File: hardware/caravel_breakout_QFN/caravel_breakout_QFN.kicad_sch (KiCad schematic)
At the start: 20 parts, among them J1 Conn_01x14_Female, J2 Conn_01x14_Female, J3 Conn_01x14_Female, J4 Conn_01x14_Female, T1 Logo, T2 Logo, U1 Caravel

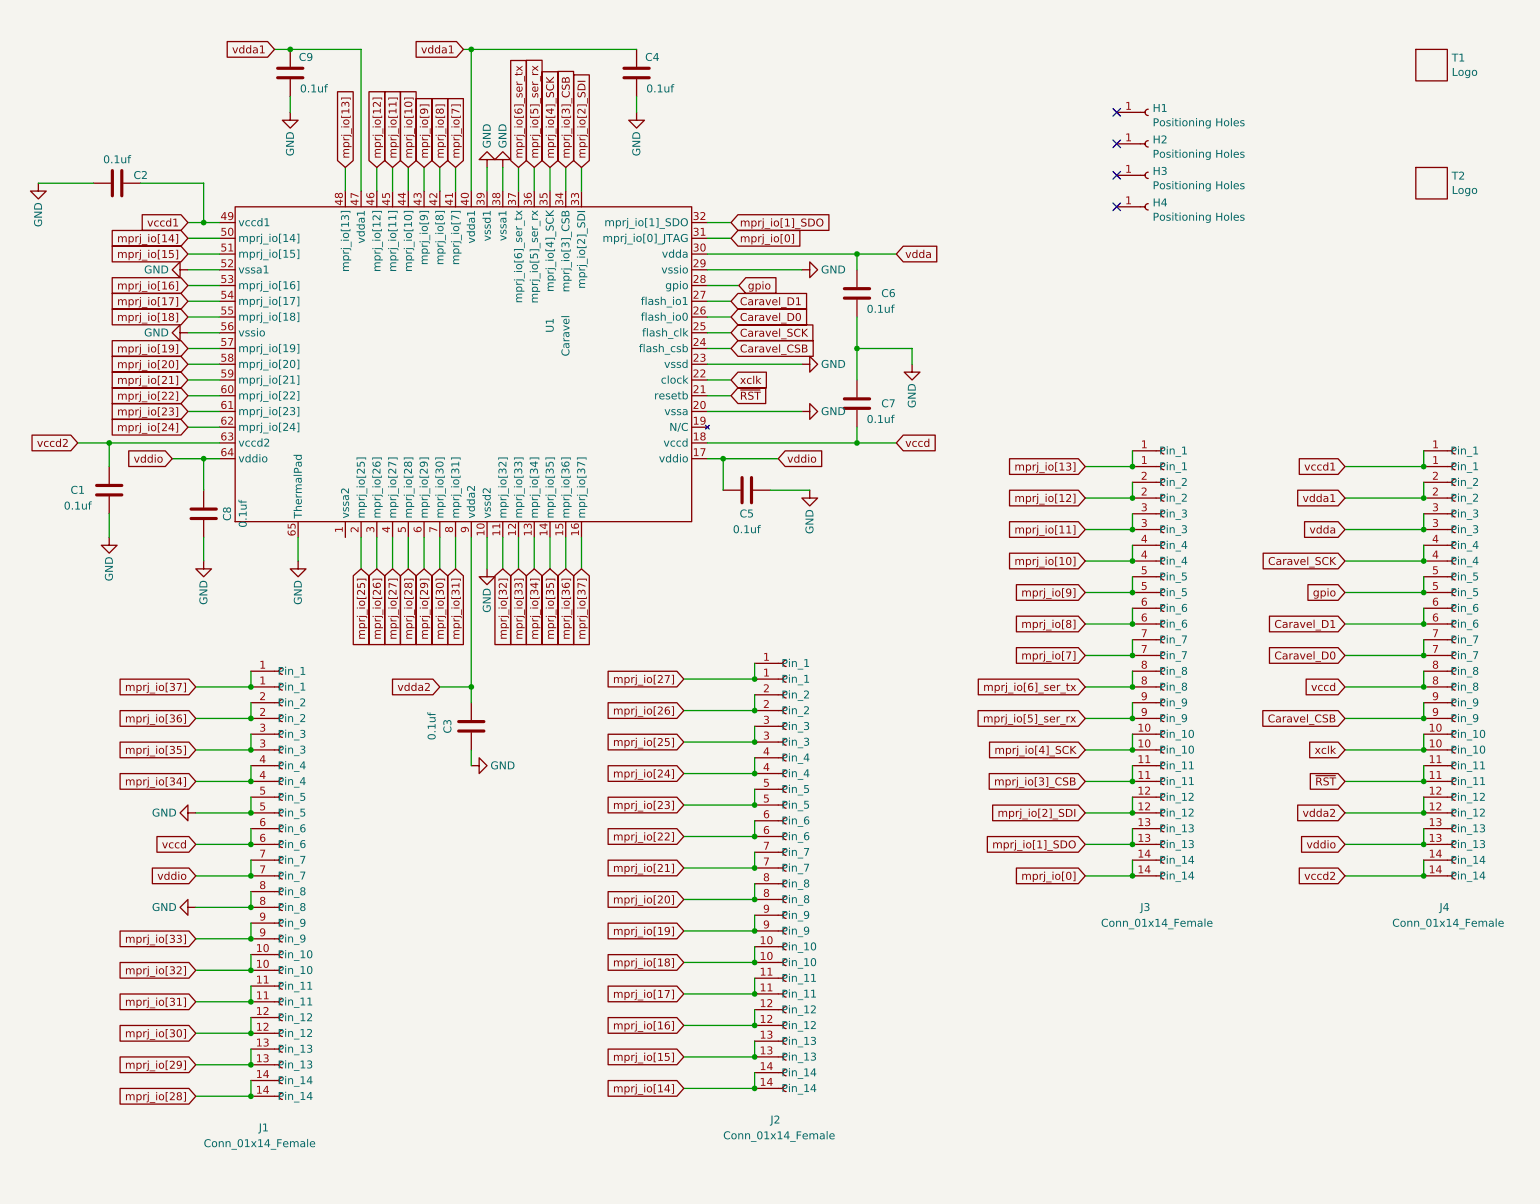
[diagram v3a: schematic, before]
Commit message: update caravel QFN breakout board with WCSP pinout (V2)
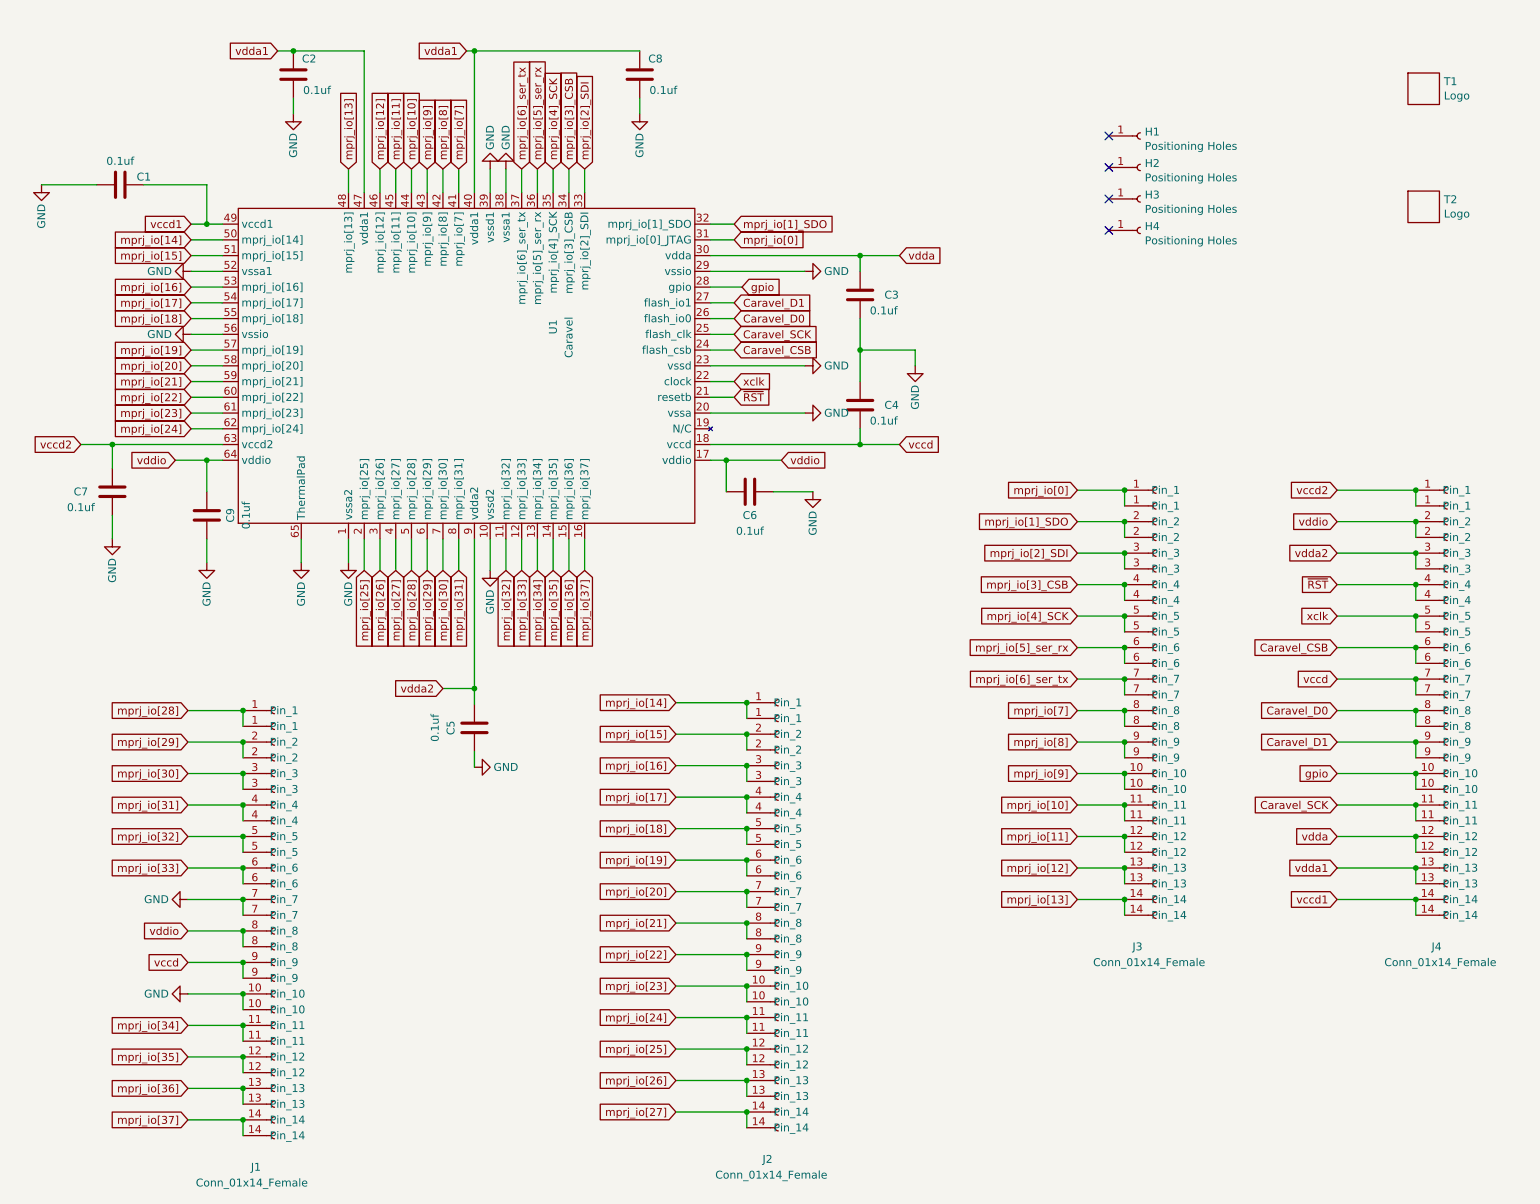
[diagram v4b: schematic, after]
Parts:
- U1: footprint Package_DFN_QFN:QFN-64-1EP_9x9mm_P0.5mm_EP7.65x7.65mm_ThermalVias -> Package_DFN_QFN:QFN-64-1EP_9x9mm_P0.5mm_EP7.65x7.65mm
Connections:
- net Caravel_CSB: now also J4.6 (Pin_6); no longer J4.9 (Pin_9)
- net Caravel_D0: now also J4.8 (Pin_8); no longer J4.7 (Pin_7)
- net Caravel_D1: now also J4.9 (Pin_9); no longer J4.6 (Pin_6)
- net Caravel_SCK: now also J4.11 (Pin_11); no longer J4.4 (Pin_4)
- net GND: now also C2.2, C3.2, C4.1, C6.1, C8.2, C9.1, J1.10 (Pin_10), J1.7 (Pin_7), U1.1 (vssa2); no longer C2.1, C3.1, C4.2, C6.2, C8.1, C9.2, J1.5 (Pin_5), J1.8 (Pin_8)
- net gpio: now also J4.10 (Pin_10); no longer J4.5 (Pin_5)
- net mprj_io[0]: now also J3.1 (Pin_1); no longer J3.14 (Pin_14)
- net mprj_io[10]: now also J3.11 (Pin_11); no longer J3.4 (Pin_4)
- net mprj_io[11]: now also J3.12 (Pin_12); no longer J3.3 (Pin_3)
- net mprj_io[12]: now also J3.13 (Pin_13); no longer J3.2 (Pin_2)
- net mprj_io[13]: now also J3.14 (Pin_14); no longer J3.1 (Pin_1)
- net mprj_io[14]: now also J2.1 (Pin_1); no longer J2.14 (Pin_14)
- net mprj_io[15]: now also J2.2 (Pin_2); no longer J2.13 (Pin_13)
- net mprj_io[16]: now also J2.3 (Pin_3); no longer J2.12 (Pin_12)
- net mprj_io[17]: now also J2.4 (Pin_4); no longer J2.11 (Pin_11)
- net mprj_io[18]: now also J2.5 (Pin_5); no longer J2.10 (Pin_10)
- net mprj_io[19]: now also J2.6 (Pin_6); no longer J2.9 (Pin_9)
- net mprj_io[1]_SDO: now also J3.2 (Pin_2); no longer J3.13 (Pin_13)
- net mprj_io[20]: now also J2.7 (Pin_7); no longer J2.8 (Pin_8)
- net mprj_io[21]: now also J2.8 (Pin_8); no longer J2.7 (Pin_7)
- net mprj_io[22]: now also J2.9 (Pin_9); no longer J2.6 (Pin_6)
- net mprj_io[23]: now also J2.10 (Pin_10); no longer J2.5 (Pin_5)
- net mprj_io[24]: now also J2.11 (Pin_11); no longer J2.4 (Pin_4)
- net mprj_io[25]: now also J2.12 (Pin_12); no longer J2.3 (Pin_3)
- net mprj_io[26]: now also J2.13 (Pin_13); no longer J2.2 (Pin_2)
- net mprj_io[27]: now also J2.14 (Pin_14); no longer J2.1 (Pin_1)
- net mprj_io[28]: now also J1.1 (Pin_1); no longer J1.14 (Pin_14)
- net mprj_io[29]: now also J1.2 (Pin_2); no longer J1.13 (Pin_13)
- net mprj_io[2]_SDI: now also J3.3 (Pin_3); no longer J3.12 (Pin_12)
- net mprj_io[30]: now also J1.3 (Pin_3); no longer J1.12 (Pin_12)
- net mprj_io[31]: now also J1.4 (Pin_4); no longer J1.11 (Pin_11)
- net mprj_io[32]: now also J1.5 (Pin_5); no longer J1.10 (Pin_10)
- net mprj_io[33]: now also J1.6 (Pin_6); no longer J1.9 (Pin_9)
- net mprj_io[34]: now also J1.11 (Pin_11); no longer J1.4 (Pin_4)
- net mprj_io[35]: now also J1.12 (Pin_12); no longer J1.3 (Pin_3)
- net mprj_io[36]: now also J1.13 (Pin_13); no longer J1.2 (Pin_2)
- net mprj_io[37]: now also J1.14 (Pin_14); no longer J1.1 (Pin_1)
- net mprj_io[3]_CSB: now also J3.4 (Pin_4); no longer J3.11 (Pin_11)
- net mprj_io[4]_SCK: now also J3.5 (Pin_5); no longer J3.10 (Pin_10)
- net mprj_io[5]_ser_rx: now also J3.6 (Pin_6); no longer J3.9 (Pin_9)
- net mprj_io[6]_ser_tx: now also J3.7 (Pin_7); no longer J3.8 (Pin_8)
- net mprj_io[7]: now also J3.8 (Pin_8); no longer J3.7 (Pin_7)
- net mprj_io[8]: now also J3.9 (Pin_9); no longer J3.6 (Pin_6)
- net mprj_io[9]: now also J3.10 (Pin_10); no longer J3.5 (Pin_5)
- net vccd: now also C4.2, J1.9 (Pin_9), J4.7 (Pin_7); no longer C7.2, J1.6 (Pin_6), J4.8 (Pin_8)
- net vccd1: now also C1.2, J4.14 (Pin_14); no longer C2.2, J4.1 (Pin_1)
- net vccd2: now also C7.2, J4.1 (Pin_1); no longer C1.2, J4.14 (Pin_14)
- net vdda: now also C3.1, J4.12 (Pin_12); no longer C6.1, J4.3 (Pin_3)
- net vdda1: now also C2.1, C8.1, J4.13 (Pin_13); no longer C4.1, C9.1, J4.2 (Pin_2)
- net vdda2: now also C5.2, J4.3 (Pin_3); no longer C3.2, J4.12 (Pin_12)
- net vddio: now also C6.2, C9.2, J1.8 (Pin_8), J4.2 (Pin_2); no longer C5.2, C8.2, J1.7 (Pin_7), J4.13 (Pin_13)
- net xclk: now also J4.5 (Pin_5); no longer J4.10 (Pin_10)
- net ~{RST}: now also J4.4 (Pin_4); no longer J4.11 (Pin_11)
